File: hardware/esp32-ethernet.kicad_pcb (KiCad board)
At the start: 4 copper layers, 80 x 40 mm, 132 parts, among them J101 USB-C-2, J301 RJSL-009TA1, P101 EXT_HEADER, P201 CON-SENSOR2, P202 CON-SENSOR2, P203 CON-SENSOR2, P204 CON-SENSOR2, P205 CON-SENSOR2, P206 CON-SENSOR2, Q101 BC817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

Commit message: change crystal
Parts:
- X301: value 25Mhz -> 25Mhz-10pF

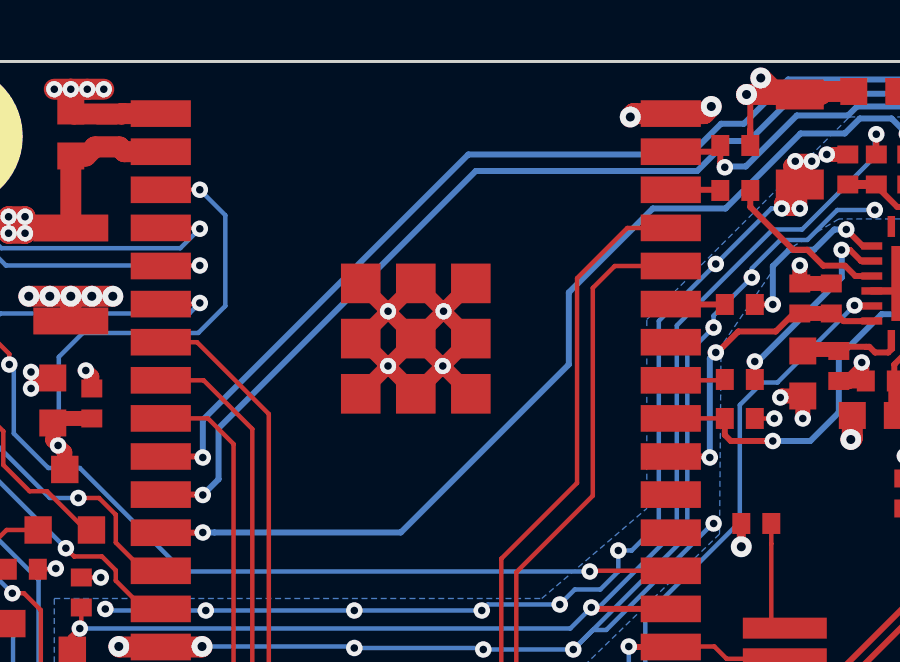
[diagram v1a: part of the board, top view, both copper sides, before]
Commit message: fix wrover footprint gnd pads
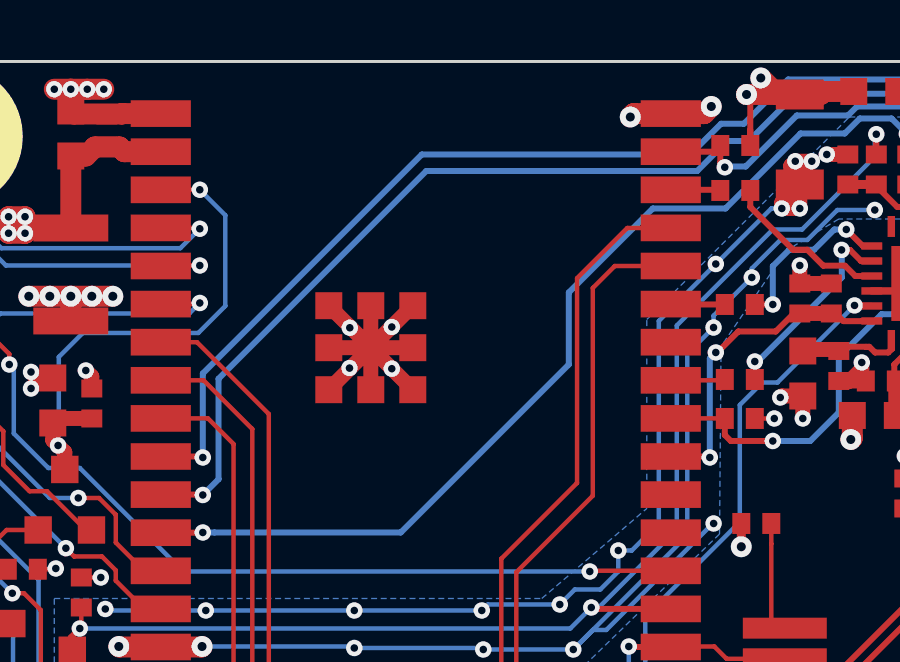
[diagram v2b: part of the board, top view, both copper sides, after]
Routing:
- net GND: track 262.3 -> 255.0 mm
- net RMII_RXD1: track 37.7 -> 38.7 mm
- net RMII_RXD0: track 35.1 -> 36.0 mm

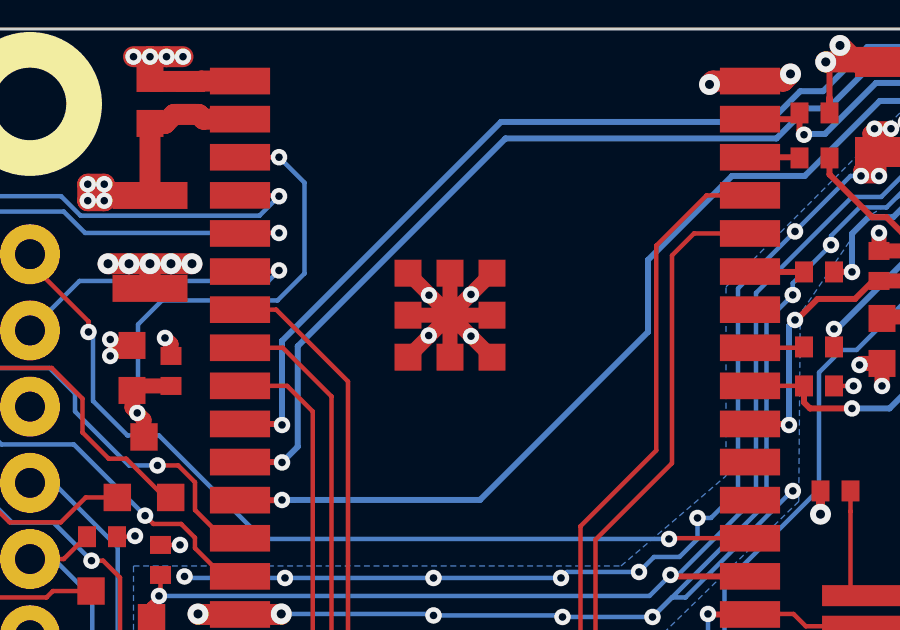
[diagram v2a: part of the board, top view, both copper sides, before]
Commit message: fix ground pad layout
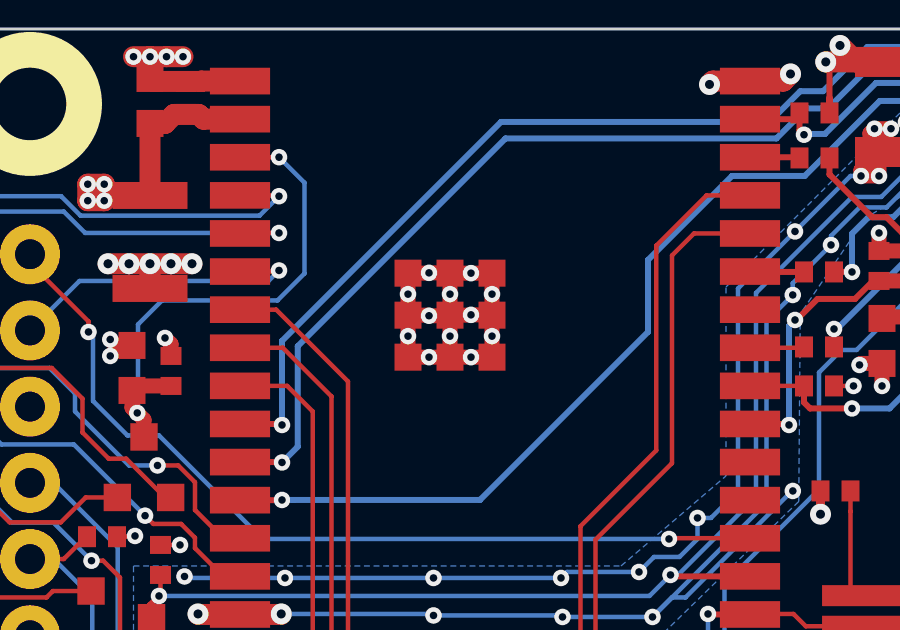
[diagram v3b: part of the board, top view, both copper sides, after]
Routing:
- net GND: track 255.0 -> 259.0 mm, vias 192 -> 200
